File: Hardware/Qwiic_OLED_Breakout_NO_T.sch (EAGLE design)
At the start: 26 parts

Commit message: Adding Gerbers
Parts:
- removed H1, H2: STAND-OFF, SparkFun-Hardware:STAND-OFF
- removed U$1: SPARKX-LOGO4, SparkX:SPARKX-LOGO4
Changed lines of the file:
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@@
 <part name="SUPPLY7" library="SparkFun-Aesthetics" deviceset="VDD" device=""/>
 <part name="GND13" library="SparkFun-Aesthetics" deviceset="GND" device=""/>
-<part name="U$1" library="SparkX" deviceset="SPARKX-LOGO" device="4" value="SPARKX-LOGO4"/>
 <part name="R3" library="SparkFun-Passives" deviceset="RESISTOR" device="0603-RES" value="10k"/>
 <part name="SUPPLY8" library="SparkFun-Aesthetics" deviceset="VDD" device=""/>
@@
 <part name="R14" library="SparkFun-Resistors" deviceset="4.7KOHM" device="-0603-1/10W-1%" value="4.7k"/>
 <part name="JP2" library="SparkFun-Jumpers" deviceset="JUMPER-SMT_3_2-NC_PASTE" device="_SILK" value=""/>
-<part name="H1" library="SparkFun-Hardware" deviceset="STAND-OFF" device=""/>
-<part name="H2" library="SparkFun-Hardware" deviceset="STAND-OFF" device=""/>
 <part name="SUPPLY2" library="SparkFun-Aesthetics" deviceset="VDD" device=""/>
 <part name="JP3" library="SparkFun-Jumpers" deviceset="JUMPER-SMT_2_NO" device="_SILK" value=""/>
@@
 <instance part="SUPPLY7" gate="VDD" x="25.4" y="93.98"/>
 <instance part="GND13" gate="1" x="25.4" y="78.74"/>
-<instance part="U$1" gate="G$1" x="134.62" y="5.08"/>
 <instance part="R3" gate="G$1" x="157.48" y="88.9" rot="MR90"/>
 <instance part="SUPPLY8" gate="VDD" x="157.48" y="96.52" rot="MR0"/>
@@
 <instance part="R14" gate="G$1" x="68.58" y="147.32" rot="R90"/>
 <instance part="JP2" gate="G$1" x="60.96" y="157.48" rot="R270"/>
-<instance part="H1" gate="G$1" x="236.22" y="33.02"/>
-<instance part="H2" gate="G$1" x="238.76" y="33.02"/>
 <instance part="SUPPLY2" gate="VDD" x="60.96" y="165.1"/>
 <instance part="JP3" gate="G$1" x="157.48" y="71.12" rot="R90"/>

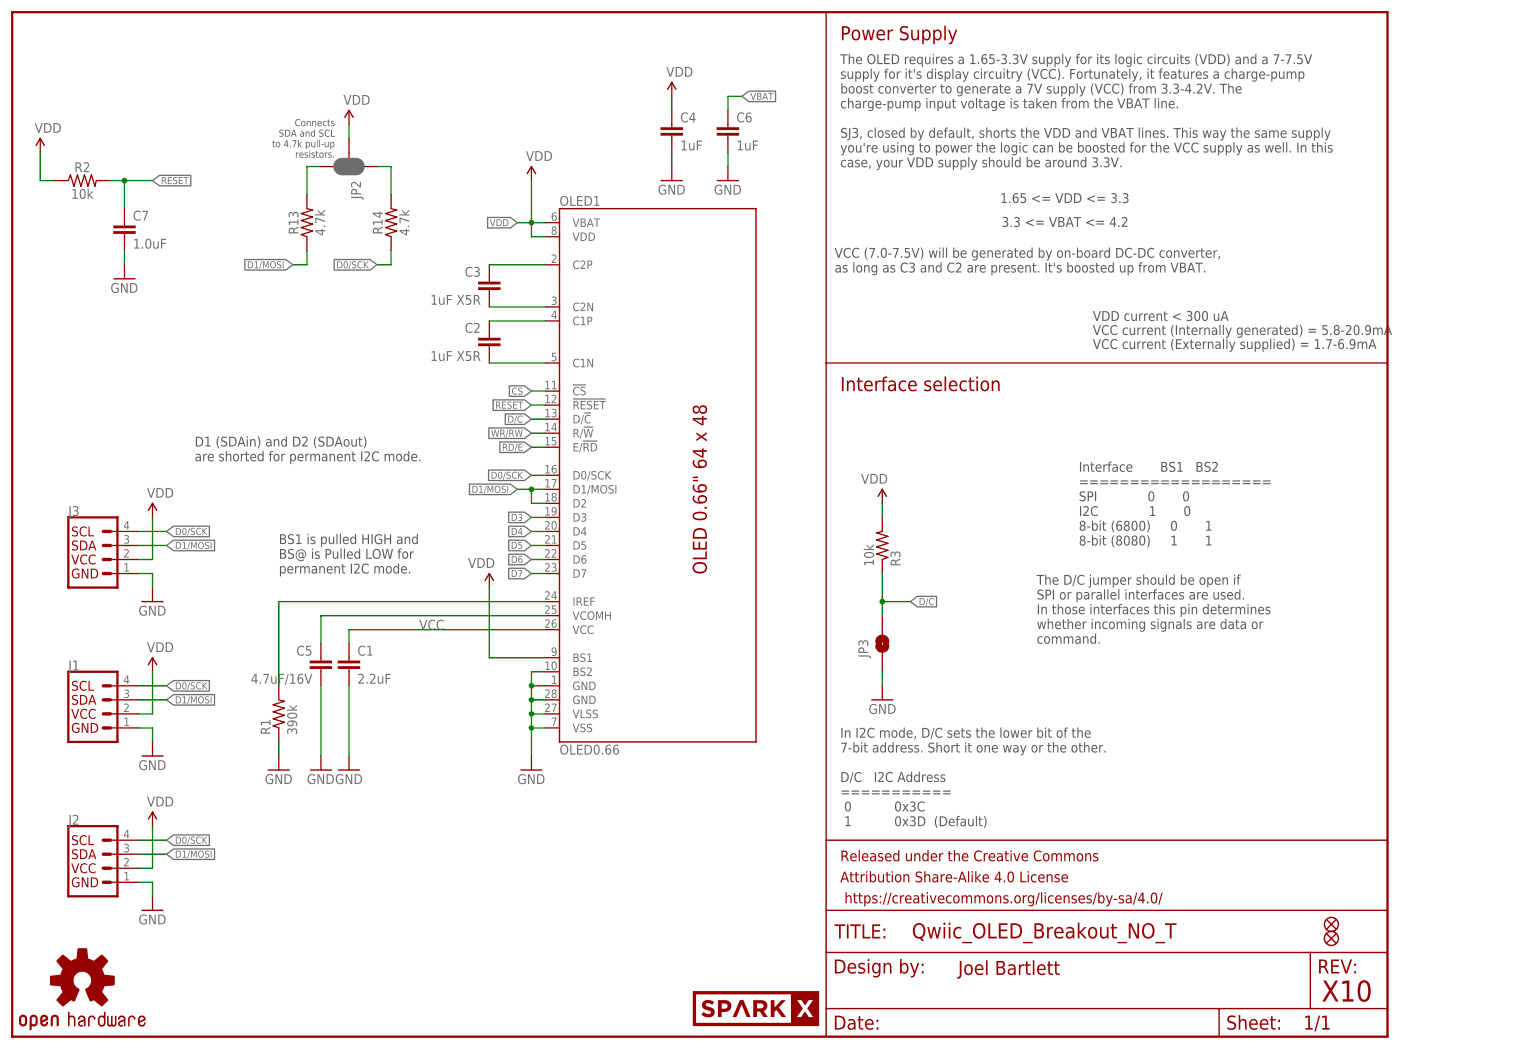
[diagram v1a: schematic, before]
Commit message: Adding product page files
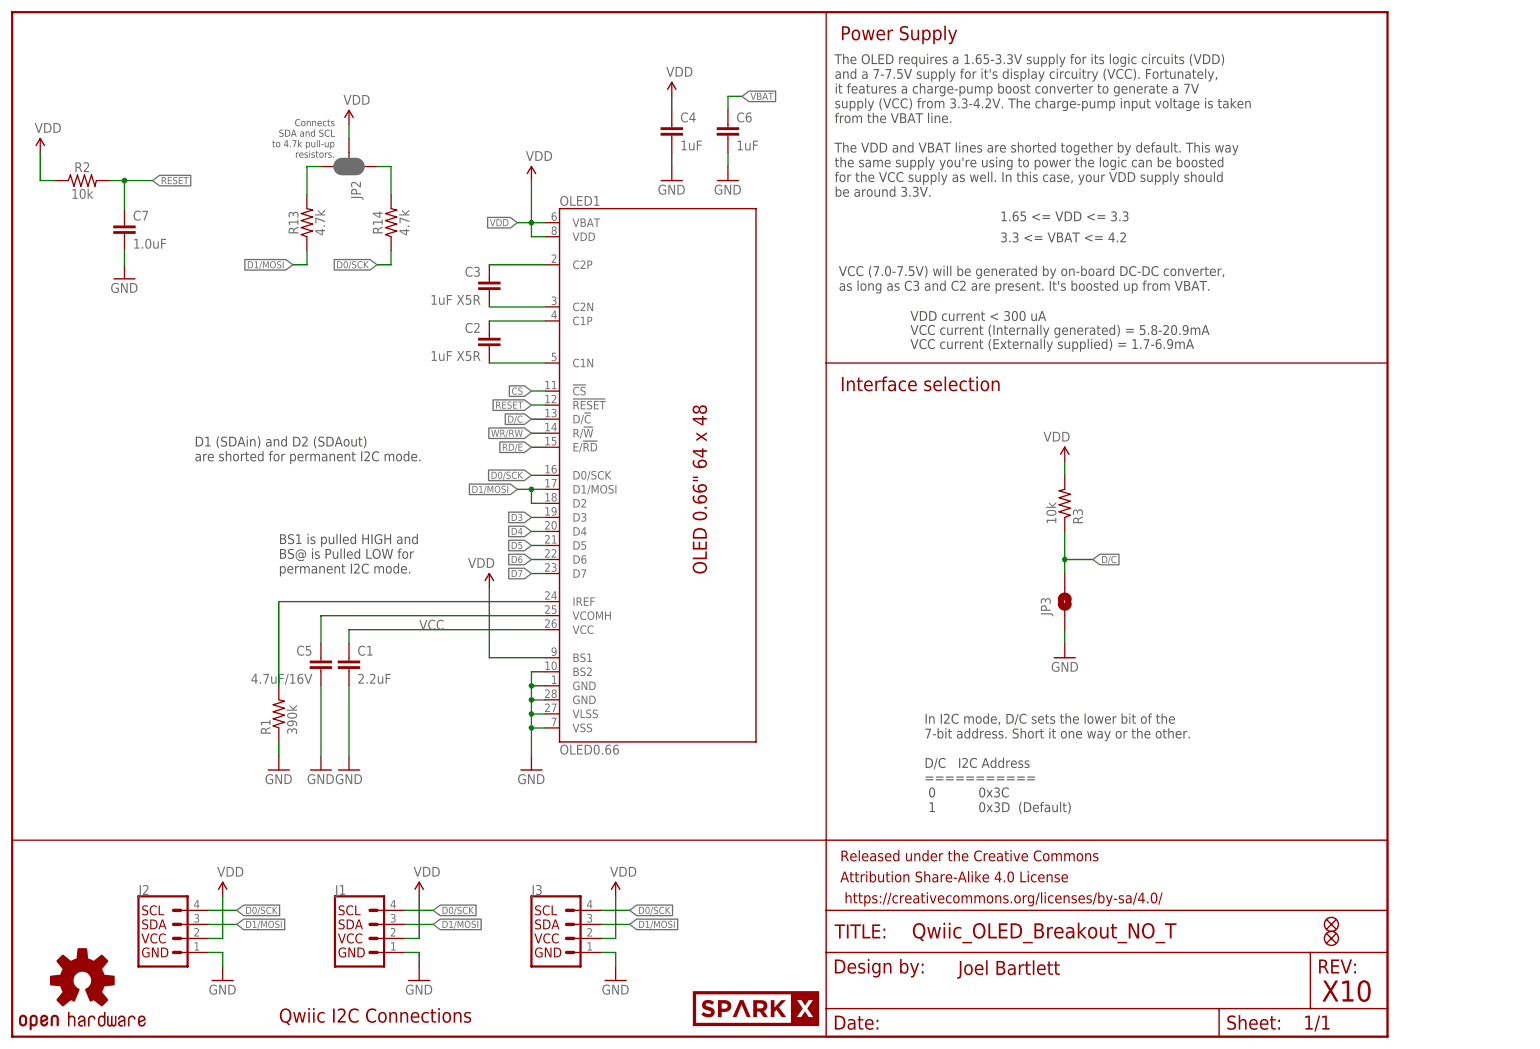
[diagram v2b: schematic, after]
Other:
- note added: "Qwiic I2C Connections"
- note added: "The OLED requires a 1.65-3.3V supply for its logic circuits (VDD) and a 7-7.5V supply for it's display circuitry (VCC). Fortunately, it features a charge-pump boost converter to generate a 7V supply (VCC) from 3.3-4.2V. The charge-pump input voltage is taken from the VBAT line. The VDD and VBAT lines are shorted together by default. This way the same supply you're using to power the logic can be 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"
- note removed: "Interface BS1 BS2 =================== SPI 0 0 I2C 1 0 8-bit (6800) 0 1 8-bit (8080) 1 1"
- note removed: "The D/C jumper should be open if SPI or parallel interfaces are used. In those interfaces this pin determines whether incoming signals are data or command."
- note removed: "The OLED requires a 1.65-3.3V supply for its logic circuits (VDD) and a 7-7.5V supply for it's display circuitry (VCC). Fortunately, it features a charge-pump boost converter to generate a 7V supply (VCC) from 3.3-4.2V. The charge-pump input voltage is taken from the VBAT line. SJ3, closed by default, shorts the VDD and VBAT lines. This way the same supply you're using to power the logic can be b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"
- moved on the sheet: J1, J2, J3, JP3, R3
